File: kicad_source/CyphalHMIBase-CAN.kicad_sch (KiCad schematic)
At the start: 47 parts, among them CN1 RASPBERRYPI_PICO, CN12 S3B-PH-SM4-TB, CN2 SM04B-SRSS-TB, CN3 SM04B-SRSS-TB, CN7 DNI, CN8 DNI, SW1 PTS636 SM43 SMTR LFS, U3 M24C64-RMN6TP

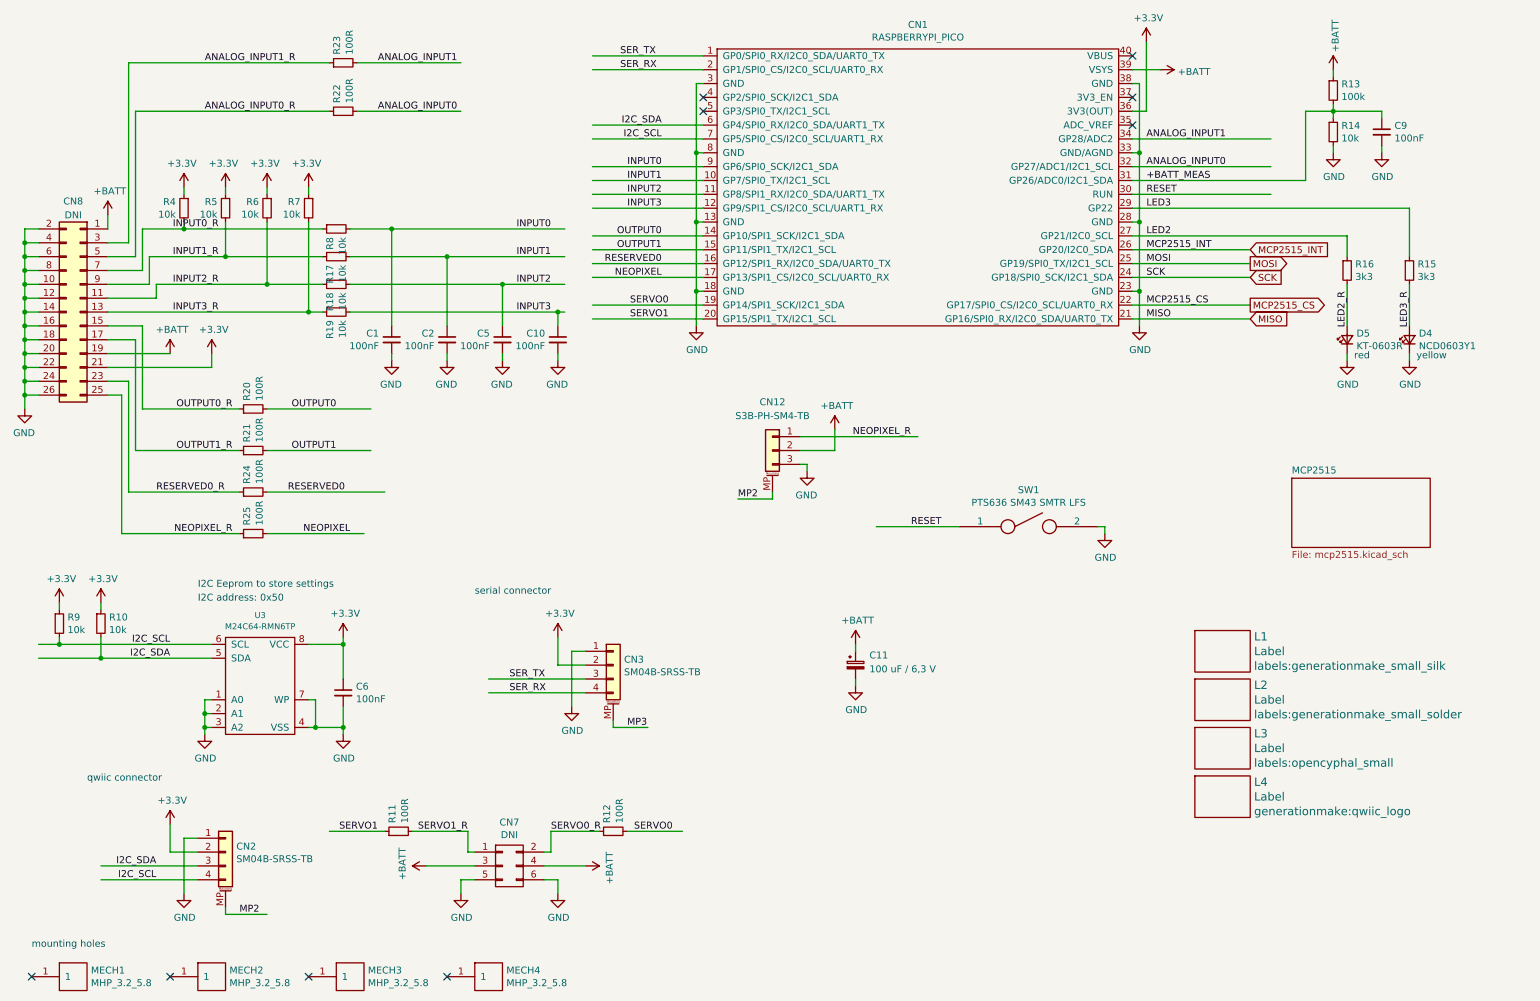
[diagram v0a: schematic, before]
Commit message: removed unnecessary parts
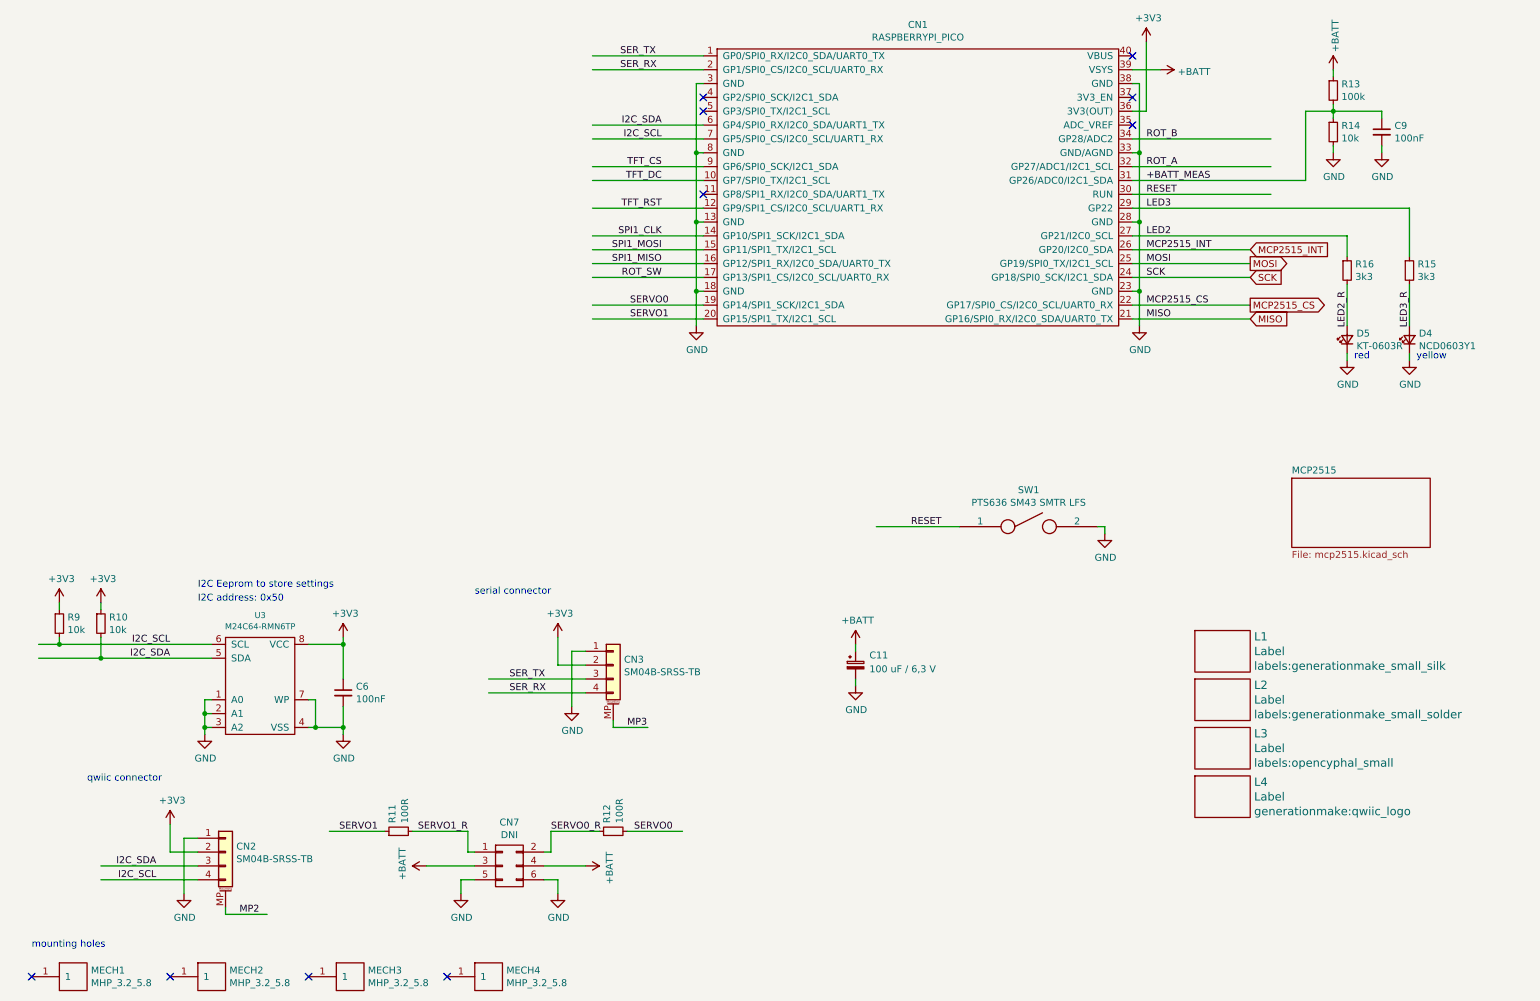
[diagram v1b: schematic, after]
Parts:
- removed C1, C10, C2, C5: 100nF, Capacitor_SMD:C_0603_1608Metric, symbol Device:C_Small
- removed CN12: S3B-PH-SM4-TB, generationmake:JST_PH_S3B-PH-SM4-TB_1x03-1MP_P2.00mm_Horizontal, symbol Connector_Generic_MountingPin:Conn_01x03_MountingPin
- removed CN8: DNI, Connector_PinHeader_2.54mm:PinHeader_2x13_P2.54mm_Vertical, symbol Connector_Generic:Conn_02x13_Odd_Even
- removed R17, R18, R19, R4, R5, R6, R7, R8: 10k, Resistor_SMD:R_0603_1608Metric, symbol Device:R_Small
- removed R20, R21, R22, R23, R24, R25: 100R, Resistor_SMD:R_0603_1608Metric, symbol Device:R_Small
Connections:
- net ANALOG_INPUT0 renamed ROT_A
- net ANALOG_INPUT1 renamed ROT_B
- net INPUT0 renamed TFT_CS
- net INPUT1 renamed TFT_DC
- net INPUT2: no longer names the net of CN1.11 (GP8/SPI1_RX/I2C0_SDA/UART1_TX)
- net INPUT3 renamed TFT_RST
- net NEOPIXEL renamed ROT_SW
- net OUTPUT0 renamed SPI1_CLK
- net OUTPUT1 renamed SPI1_MOSI
- net RESERVED0 renamed SPI1_MISO
- no-connect marks 9 -> 10
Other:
- title: CyphalPicoBase/CAN -> CyphalIMUBase/CAN
